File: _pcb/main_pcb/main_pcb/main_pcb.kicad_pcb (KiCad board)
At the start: 2 copper layers, 58 parts, among them J1 Conn_01x01_Pin, J2 Conn_01x01_Pin, SW1 SW_Push, SW2 SW_Push, SW3 SW_Push, SW4 SW_Push, SW5 SW_Push, SW6 SW_Push, SW7 SW_Push, SW8 SW_Push, U1 Pico, U2 74HC4051, U3 PCF8574A, U4 PCF8574A

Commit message: positoned all but pico
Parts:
- C1, C10, C2, C3, C4, C9, R10, R22, R23, R24, R25, R26, R27, R28, R29, R5, R6, R7, R8, R9, U2, U3, U4: moved to B.Cu
- moved SW2 459.6 mm to (238.8, 68.6)
- moved SW1 442.7 mm to (238.8, 88.9)
- moved SW4 429.5 mm to (218.4, 68.6)
- moved SW3 411.3 mm to (218.4, 88.9)
- moved D15 389.4 mm to (233.7, 78.7)
- moved R28 388.3 mm to (240.4, 78.7)
- moved D16 380.8 mm to (233.7, 99.1)
- moved R29 379.6 mm to (240.4, 99.1)
- moved SW7 379.2 mm to (198.1, 68.6)
- moved SW8 376.2 mm to (198.1, 88.9)
- moved U3 375.4 mm to (217.2, 111.4), turned to 90 degrees
- moved SW5 375.0 mm to (177.8, 68.6)
- moved SW6 371.9 mm to (177.8, 88.9)
- moved D13 368.4 mm to (213.4, 78.7)
- moved R26 367.5 mm to (220.1, 78.7)
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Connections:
- SW5 pad 2: Net-(U3-P4) -> Net-(U4-P3)
- SW6 pad 2: Net-(U3-P5) -> Net-(U4-P2)
- SW7 pad 2: Net-(U3-P6) -> Net-(U4-P1)
- SW8 pad 2: Net-(U3-P7) -> Net-(U4-P0)
- U3 pad 10: Net-(U3-P5) -> Net-(D14-K)
- U3 pad 11: Net-(U3-P6) -> Net-(D15-K)
- U3 pad 12: Net-(U3-P7) -> Net-(D16-K)
- U3 pad 9: Net-(U3-P4) -> Net-(D13-K)
- U4 pad 4: Net-(D16-K) -> Net-(U4-P0)
- U4 pad 5: Net-(D15-K) -> Net-(U4-P1)
- U4 pad 6: Net-(D14-K) -> Net-(U4-P2)
- U4 pad 7: Net-(D13-K) -> Net-(U4-P3)

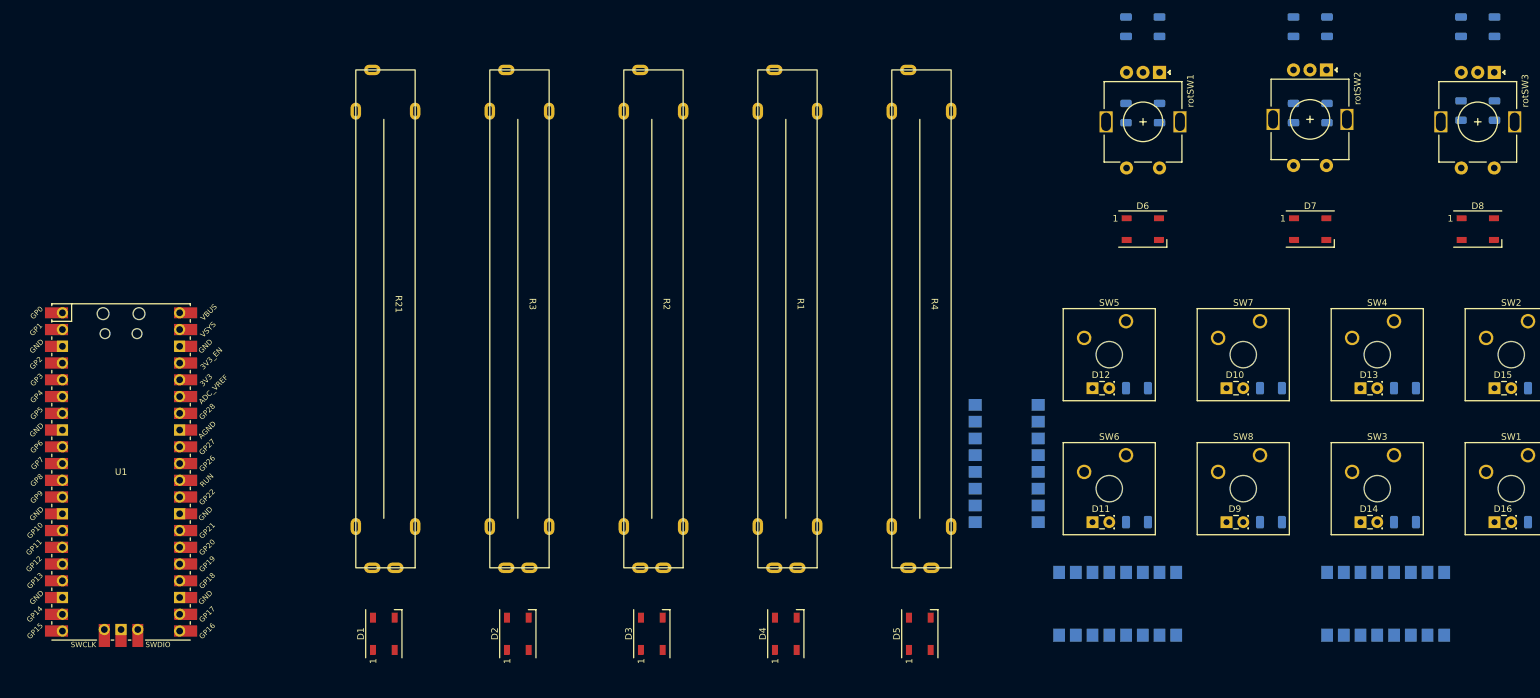
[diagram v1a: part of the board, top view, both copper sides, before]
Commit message: position of pico not really clear
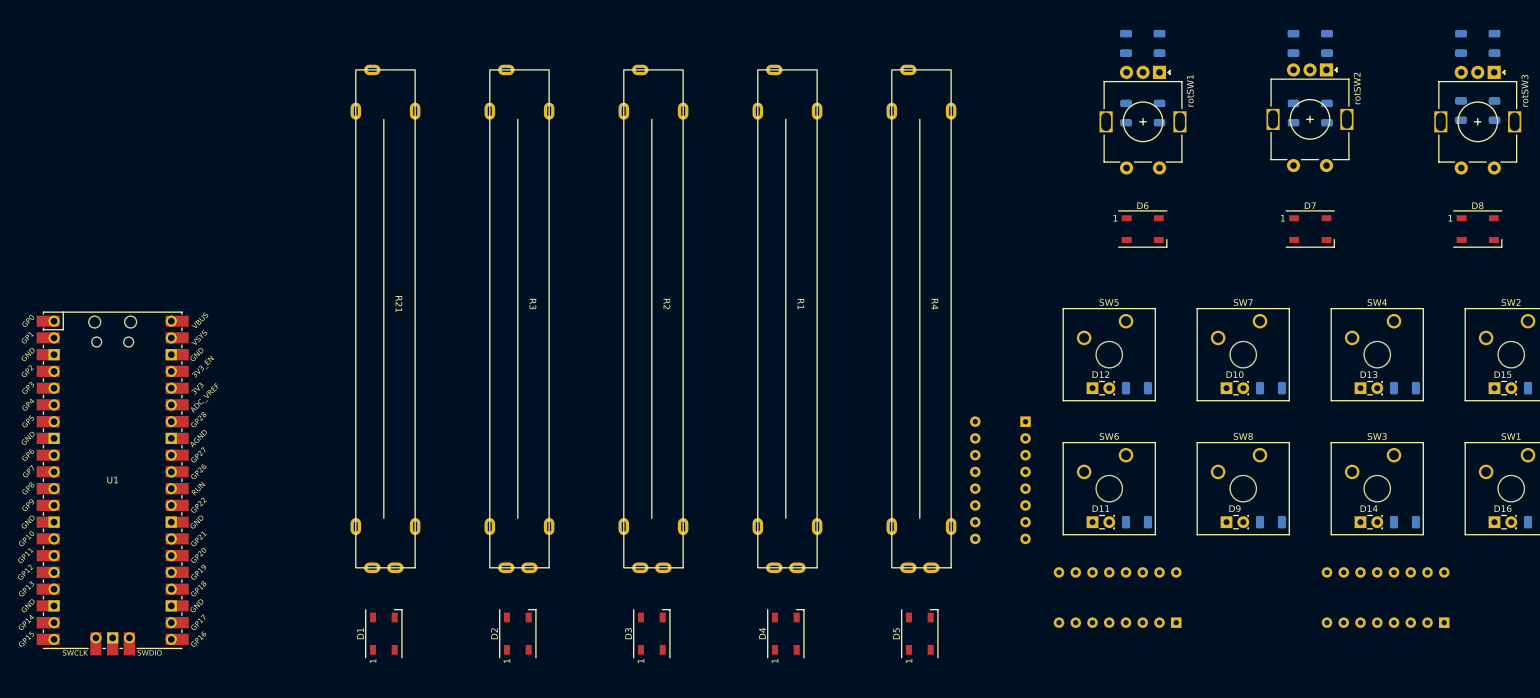
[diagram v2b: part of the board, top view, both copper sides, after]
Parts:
- U2, U3, U4: footprint Package_DIP:SMDIP-16_W9.53mm -> Package_DIP:DIP-16_W7.62mm
- moved U3 9.34 mm to (226.1, 114.3)
- moved U4 9.34 mm to (185.4, 114.3)
- moved U2 6.96 mm to (162.6, 83.8)
- moved C1 2.54 mm to (177.8, 26.5)
- moved C10 2.54 mm to (203.2, 26.5)
- moved C2 2.54 mm to (182.9, 26.5)
- moved C3 2.54 mm to (228.6, 26.5)
- moved C4 2.54 mm to (233.7, 26.5)
- moved C9 2.54 mm to (208.3, 26.5)
- moved U1 1.80 mm to (24.1, 92.7)
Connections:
- U1 pad 24: ADC_MUL_PLEX_GPIO_0 -> ADC_MUL_PLEX_GPIO_2
- U1 pad 26: ADC_MUL_PLEX_GPIO_2 -> ADC_MUL_PLEX_GPIO_0

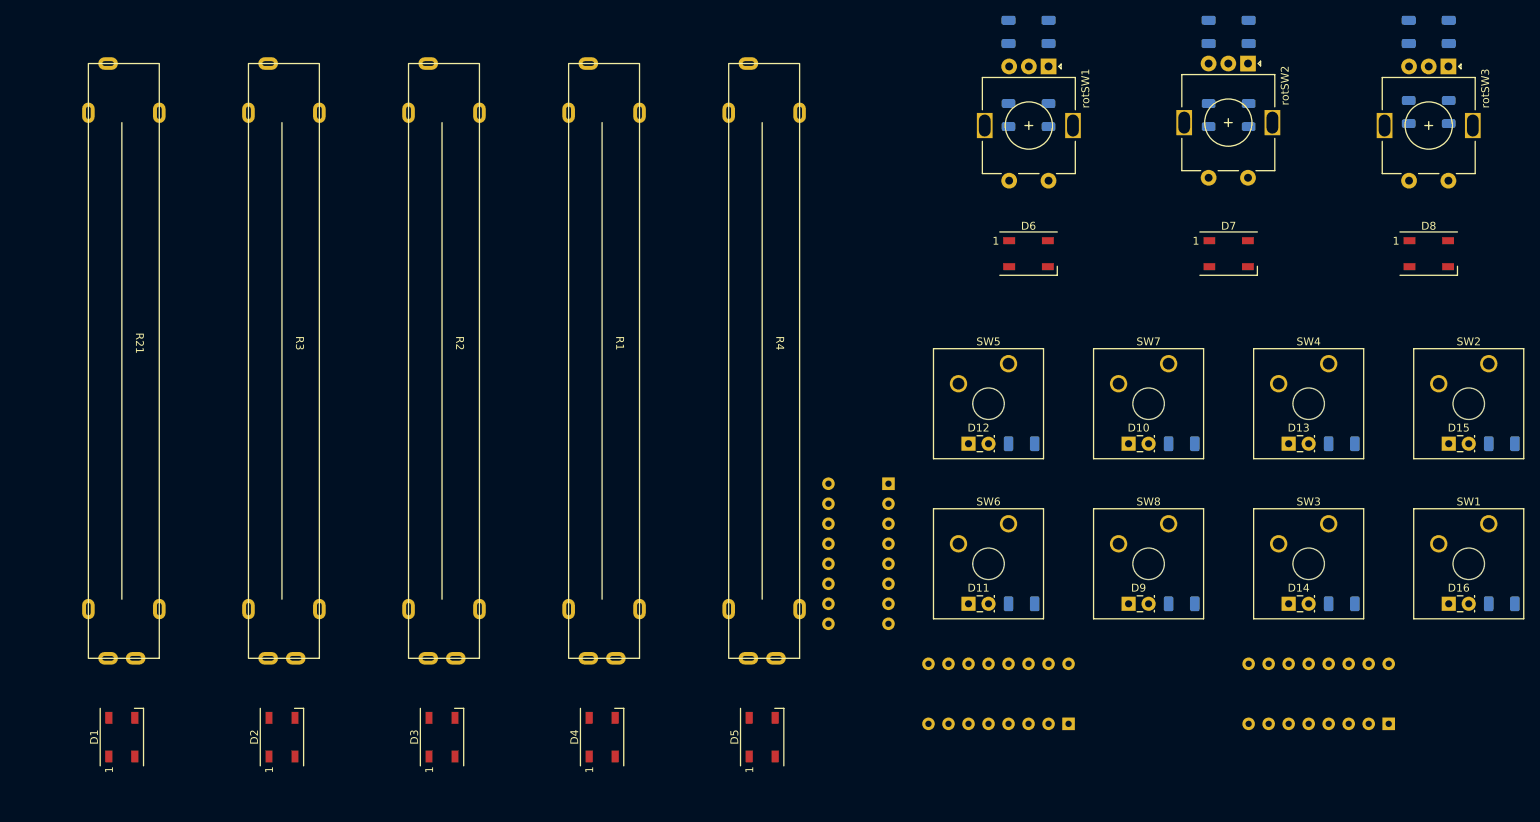
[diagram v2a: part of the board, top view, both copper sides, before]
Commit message: alle anderen Verbindungen mit Lackdraht
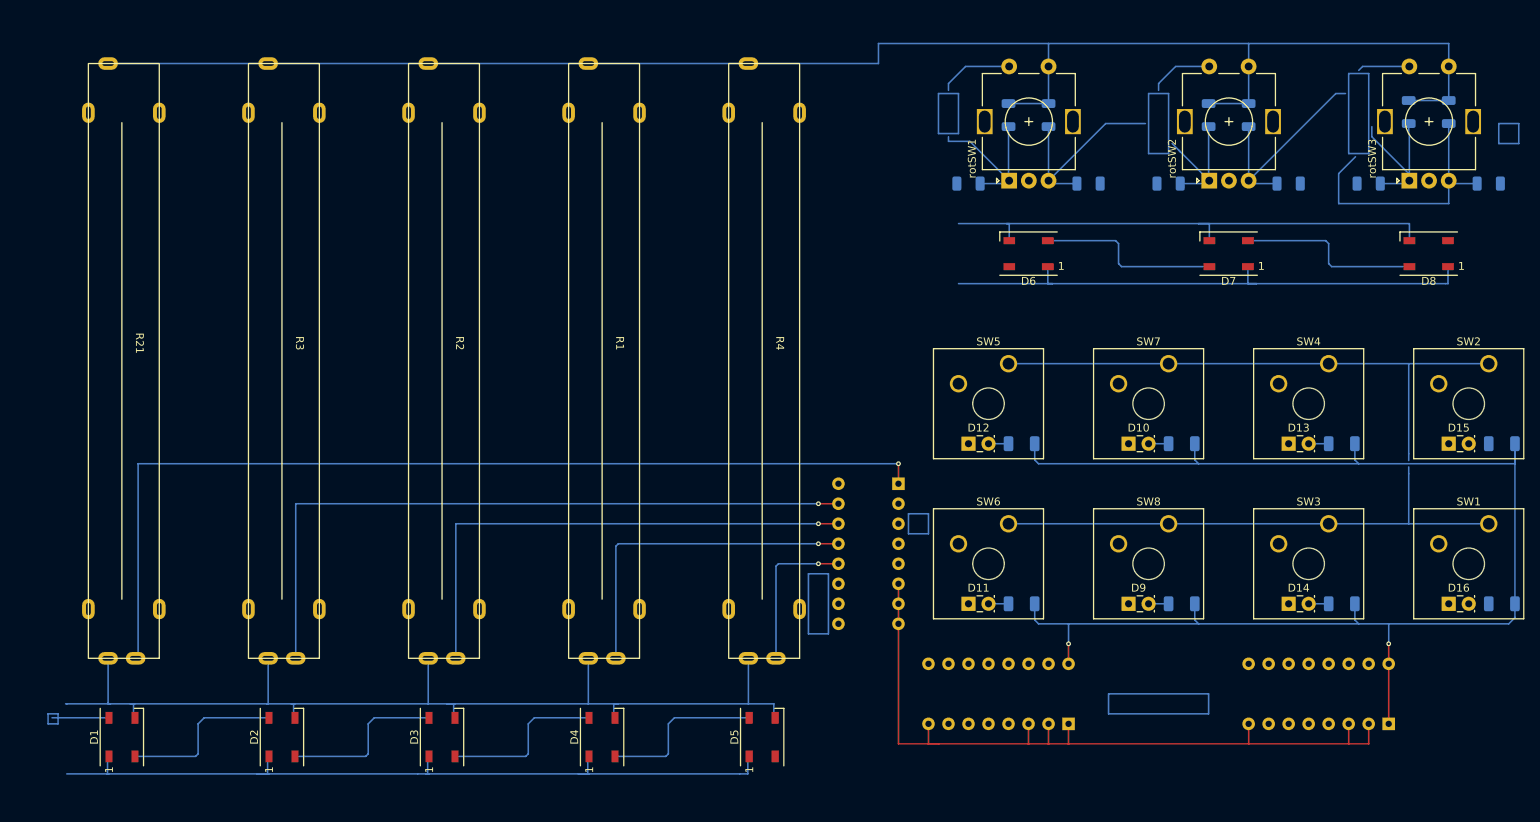
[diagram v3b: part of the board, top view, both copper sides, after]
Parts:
- moved C10 21.8 mm to (213.4, 45.7), turned to 180 degrees
- moved C1 21.8 mm to (188.0, 45.7), turned to 180 degrees
- moved C2 21.8 mm to (172.7, 45.7), turned to 180 degrees
- moved C9 21.8 mm to (198.1, 45.7), turned to 180 degrees
- moved C3 19.9 mm to (223.5, 45.7), turned to 180 degrees
- moved C4 19.9 mm to (238.8, 45.7), turned to 180 degrees
- moved rotSW2 15.7 mm to (203.3, 45.4), turned to 90 degrees
- moved rotSW1 15.3 mm to (177.9, 45.4), turned to 90 degrees
- moved rotSW3 15.3 mm to (228.7, 45.4), turned to 90 degrees
- moved R10 5.08 mm to (233.7, 36.6), turned to -90 degrees
- moved R5 5.08 mm to (203.2, 37.0), turned to 90 degrees
- moved R6 5.08 mm to (208.3, 37.0), turned to -90 degrees
- moved R9 5.08 mm to (228.6, 36.6), turned to 90 degrees
- moved R7 5.08 mm to (177.8, 37.0), turned to 90 degrees
- moved R8 5.08 mm to (182.9, 37.0), turned to -90 degrees
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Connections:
- R1 pad 1: 3.3 V -> GND
- R1 pad 3: GND -> 3.3 V
- R2 pad 1: 3.3 V -> GND
- R2 pad 3: GND -> 3.3 V
- R21 pad 1: 3.3 V -> GND
- R21 pad 3: GND -> 3.3 V
- R3 pad 1: 3.3 V -> GND
- R3 pad 3: GND -> 3.3 V
- R4 pad 1: 3.3 V -> GND
- R4 pad 3: GND -> 3.3 V
- U3 pad 1: GND -> 3.3 V
- U4 pad 1: 3.3 V -> GND
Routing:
- net GND: track 0.00 -> 435.9 mm
- net 3.3 V: track 0.00 -> 390.6 mm, vias 0 -> 2
- net 5 V: track 0.00 -> 170.9 mm
- net Net-(U2-A4): track 0.00 -> 123.9 mm, vias 0 -> 1
- net Net-(U2-A2): track 0.00 -> 88.5 mm, vias 0 -> 1
- net Net-(U2-A1): track 0.00 -> 65.7 mm, vias 0 -> 1
- net Net-(U2-A0): track 0.00 -> 42.6 mm, vias 0 -> 1
- net Rotary_SW_CLK_3: track 0.00 -> 34.7 mm
- net Rotary_SW_CLK_2: track 0.00 -> 27.5 mm
- net Rotary_SW_CLK_1: track 0.00 -> 25.9 mm
- net Net-(D7-DOUT): track 0.00 -> 23.4 mm
- net Net-(D6-DOUT): track 0.00 -> 23.4 mm
- net Net-(D4-DOUT): track 0.00 -> 21.3 mm
- net Net-(D2-DOUT): track 0.00 -> 21.3 mm
- net Net-(D3-DOUT): track 0.00 -> 21.3 mm
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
